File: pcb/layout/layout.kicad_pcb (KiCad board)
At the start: 2 copper layers, 102 parts, among them J1 B2B-PH-K-S, J3 B2B-PH-K-S, J4 104031-0811, Q1 AO3400A, SW1 PTS841GKSMTR LFS, SW2 JS202011AQN, U1 113991114, U3 MAX17048G+T10, U4 BMI270, U5 TPS61023DRLR, U6 AP2112K-3.3TRG1, U7 TPS22918DBVR

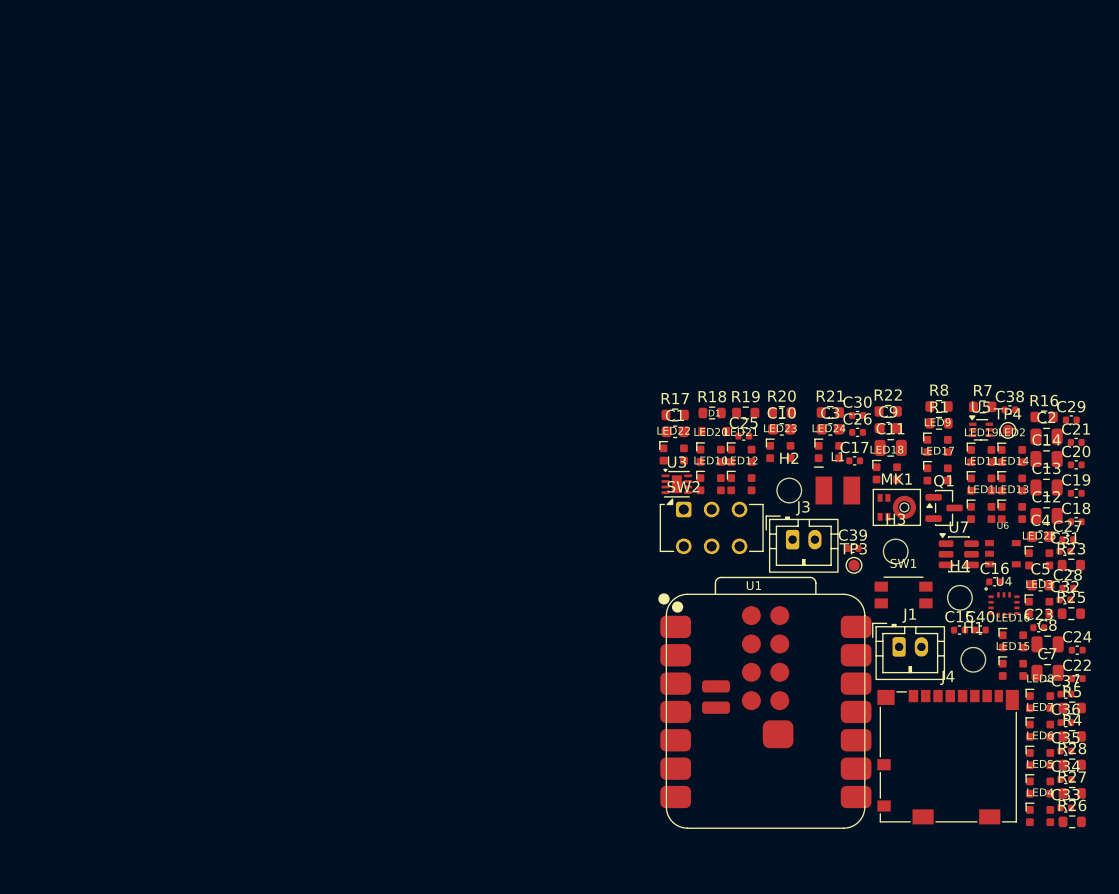
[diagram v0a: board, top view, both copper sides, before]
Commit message: Add compact placement candidate and update BOM, layout, and component library
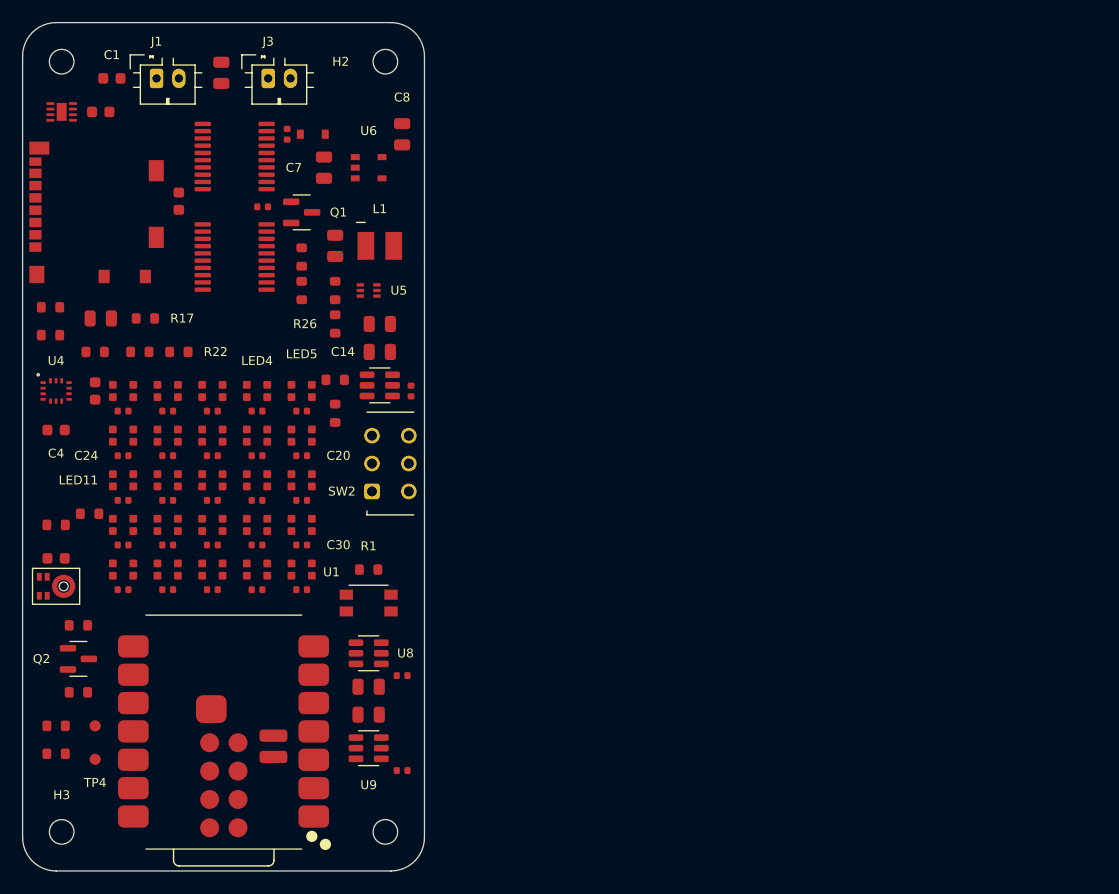
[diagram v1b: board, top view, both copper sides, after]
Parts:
- added C41: GRM1555C1E102JA01D, stdlib_kicad-footprints_Capacitor_SMD:C_0402_1005Metric, F.Cu at (116.0, 102.5)
- added C42: GRM1555C1E102JA01D, stdlib_kicad-footprints_Capacitor_SMD:C_0402_1005Metric, F.Cu at (116.0, 111.0)
- added C43: CC0805KRX5R8BB106, stdlib_kicad-footprints_Capacitor_SMD:C_0805_2012Metric, F.Cu at (113.0, 103.5)
- added C44: CC0805KRX5R8BB106, stdlib_kicad-footprints_Capacitor_SMD:C_0805_2012Metric, F.Cu at (113.0, 106.0)
- added C45: GRM155R71C104KA88D, stdlib_kicad-footprints_Capacitor_SMD:C_0402_1005Metric, F.Cu at (105.7, 54.0)
- added C46: GRM155R71C104KA88D, stdlib_kicad-footprints_Capacitor_SMD:C_0402_1005Metric, F.Cu at (103.5, 60.5)
- added Q2: AO3400A, embedr_ai_pendant_recorder_components_ao3400a_assets:SOT-23, F.Cu at (87.0, 101.0)
- added R29: RC0603FR-07100KL, stdlib_kicad-footprints_Resistor_SMD:R_0603_1608Metric, F.Cu at (87.0, 98.0)
- added R30: RC0603FR-074K7L, stdlib_kicad-footprints_Resistor_SMD:R_0603_1608Metric, F.Cu at (87.0, 104.0)
- added U10: SN74CBTLV3245APWR, embedr_ai_pendant_recorder_components_sn74cbtlv3245a:TSSOP-20, F.Cu at (101.0, 56.0)
- added U11: SN74CBTLV3245APWR, embedr_ai_pendant_recorder_components_sn74cbtlv3245a:TSSOP-20, F.Cu at (101.0, 65.0)
- added U8: TPS22918DBVR, embedr_ai_pendant_recorder_components_tps22918_assets:SOT-23-6, F.Cu at (113.0, 100.5)
- added U9: TPS22918DBVR, embedr_ai_pendant_recorder_components_tps22918_assets:SOT-23-6, F.Cu at (113.0, 109.0)
- moved H1 97.7 mm to (85.5, 47.5)
- moved R5 91.1 mm to (85.0, 109.5)
- moved R4 91.0 mm to (85.0, 107.0)
- moved J4 90.6 mm to (88.6, 61.0), turned to 90 degrees
- moved R16 89.0 mm to (85.0, 89.0)
- moved C4 88.7 mm to (85.0, 80.5)
- moved R23 88.1 mm to (88.0, 88.0)
- moved C24 87.2 mm to (91.0, 82.8)
- moved U4 87.1 mm to (85.0, 77.0)
- moved C34 87.0 mm to (91.0, 90.8)
- moved TP4 86.9 mm to (88.5, 110.0)
- moved C5 86.5 mm to (88.5, 77.0), turned to 90 degrees
- moved C35 85.7 mm to (91.0, 94.8)
- moved C33 83.8 mm to (95.0, 90.8)
- moved J1 83.8 mm to (94.0, 49.0)
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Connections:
- C12 pad 1: VBAT -> VBAT_PERIPH
- C7 pad 1: VBAT -> VBAT_PERIPH
- L1 pad 1: VBAT -> VBAT_PERIPH
- R1 pad 2: V3V3 -> V3V3_AON
- SW2 pad 4: SW2.POLE2_THROW_A -> GND
- SW2 pad 5: SW2.POLE2_COMMON -> RUN_ENABLE
- SW2 pad 6: SW2.POLE2_THROW_B -> V3V3_AON
- U1 pad 1: HAPTIC_DRIVE -> HOST_HAPTIC
- U1 pad 10: SD_MISO -> HOST_SD_MISO
- U1 pad 11: SD_MOSI -> HOST_SD_MOSI
- U1 pad 12: V3V3 -> V3V3_AON
- U1 pad 15: PDM_DATA -> HOST_PDM_DATA
- U1 pad 16: IMU_INT -> HOST_IMU_INT
- U1 pad 19: PDM_CLK_MCU -> HOST_PDM_CLK
- U1 pad 20: SD_CS -> HOST_SD_CS
- U1 pad 3: LED_ENABLE -> HOST_LED_ENABLE
- U1 pad 4: LED_DATA_MCU -> HOST_LED_DATA
- U1 pad 5: FG_SDA -> HOST_SDA
- U1 pad 6: FG_SCL -> HOST_SCL
- U1 pad 9: SD_CLK_MCU -> HOST_SD_CLK
- U5 pad 3: VBAT -> VBAT_PERIPH
- U6 pad 1: VBAT -> VBAT_PERIPH
- U6 pad 3: VBAT -> VBAT_PERIPH
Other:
- board outline added: 36 x 76 mm

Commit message: Add compact rear‑ESP candidate and update mechanical, BOM, and layout
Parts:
- J1, J3, U1: moved to B.Cu
- moved U1 20.8 mm to (88.1, 97.0), turned to 0 degrees
- turned J1 to 180 degrees
- turned J3 to 180 degrees

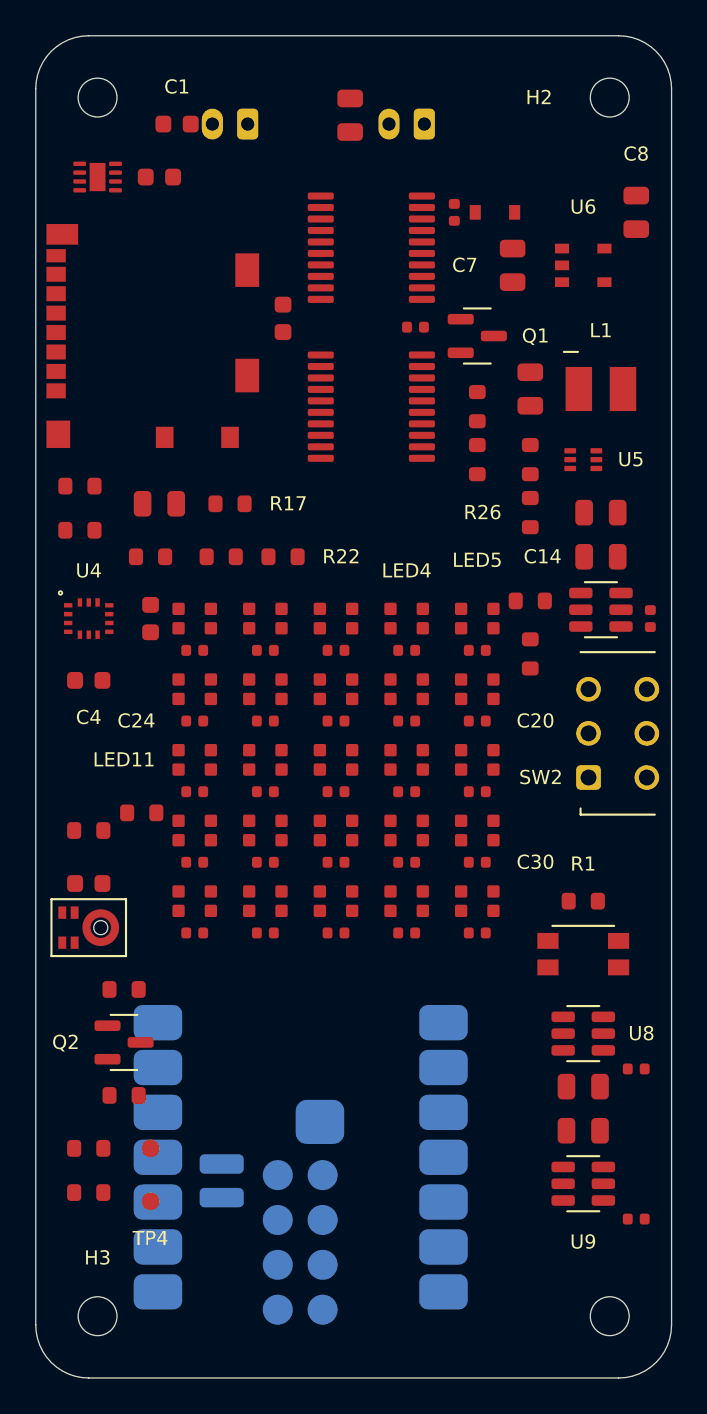
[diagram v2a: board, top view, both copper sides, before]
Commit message: Revise eyelet to slim side‑profile U‑loop with X‑directed chain
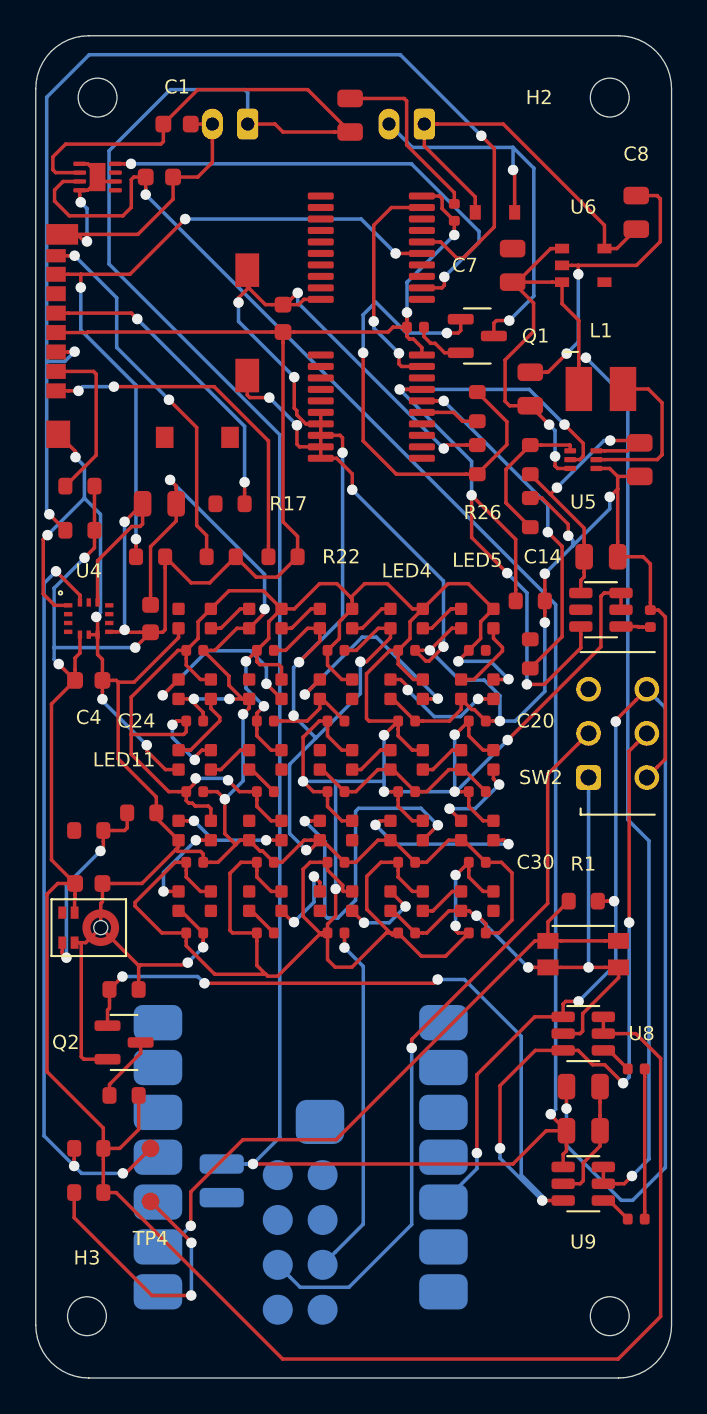
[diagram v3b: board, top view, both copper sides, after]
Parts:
- moved C13 3.72 mm to (116.2, 68.0), turned to -90 degrees
- moved H3 0.60 mm to (84.9, 116.5)
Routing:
- net GND: track 0.00 -> 452.5 mm, vias 0 -> 40
- net LED_5V: track 0.00 -> 229.1 mm, vias 0 -> 17
- net VBAT: track 0.00 -> 197.5 mm, vias 0 -> 3
- net V3V3: track 0.00 -> 192.1 mm, vias 0 -> 7
- net VBAT_PERIPH: track 0.00 -> 78.3 mm, vias 0 -> 4
- net RUN_ENABLE: track 0.00 -> 74.7 mm, vias 0 -> 7
- net V3V3_AON: track 0.00 -> 74.6 mm, vias 0 -> 5
- net FG_SDA: track 0.00 -> 70.4 mm, vias 0 -> 5
- net SD_MOSI: track 0.00 -> 66.0 mm, vias 0 -> 3
- net LED_ENABLE: track 0.00 -> 46.3 mm, vias 0 -> 5
- net MCU_EN: track 0.00 -> 41.5 mm, vias 0 -> 1
- net SD_MISO: track 0.00 -> 40.1 mm, vias 0 -> 4
- net RECORD_BUTTON: track 0.00 -> 37.1 mm, vias 0 -> 1
- net MOTOR_GATE: track 0.00 -> 27.7 mm, vias 0 -> 2
- net MOTOR_N: track 0.00 -> 23.8 mm, vias 0 -> 2
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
